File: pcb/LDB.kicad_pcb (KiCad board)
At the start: 2 copper layers, 77.2 x 50.8 mm, 79 parts, among them J1 Conn_01x10_Socket, J10 Conn_01x04_Socket, J11 Conn_01x03_Pin, J12 Conn_01x03_Pin, J13 Conn_01x03_Pin, J14 Conn_01x10_Socket, J2 Conn_01x02_Pin, J3 Conn_01x10_Socket, J4 Conn_02x02_Counter_Clockwise, J5 Conn_02x02_Counter_Clockwise, J6 Conn_02x02_Counter_Clockwise, J7 Conn_02x02_Counter_Clockwise, J8 Conn_02x02_Counter_Clockwise, J9 Conn_02x02_Counter_Clockwise, Q1 MMBFJ113, Q10 MMBFJ113, Q11 MMBFJ113, Q12 MMBFJ113, Q13 MMBFJ113, Q14 MMBFJ113, Q15 MMBFJ113, Q16 MMBFJ113, Q17 MMBFJ113, Q2 MMBFJ113, Q3 MMBFJ113, Q4 MMBFJ113, Q5 MMBFJ113, Q6 MMBFJ113, Q7 MMBFJ113, Q8 MMBFJ113, Q9 MMBFJ113, U1 4543

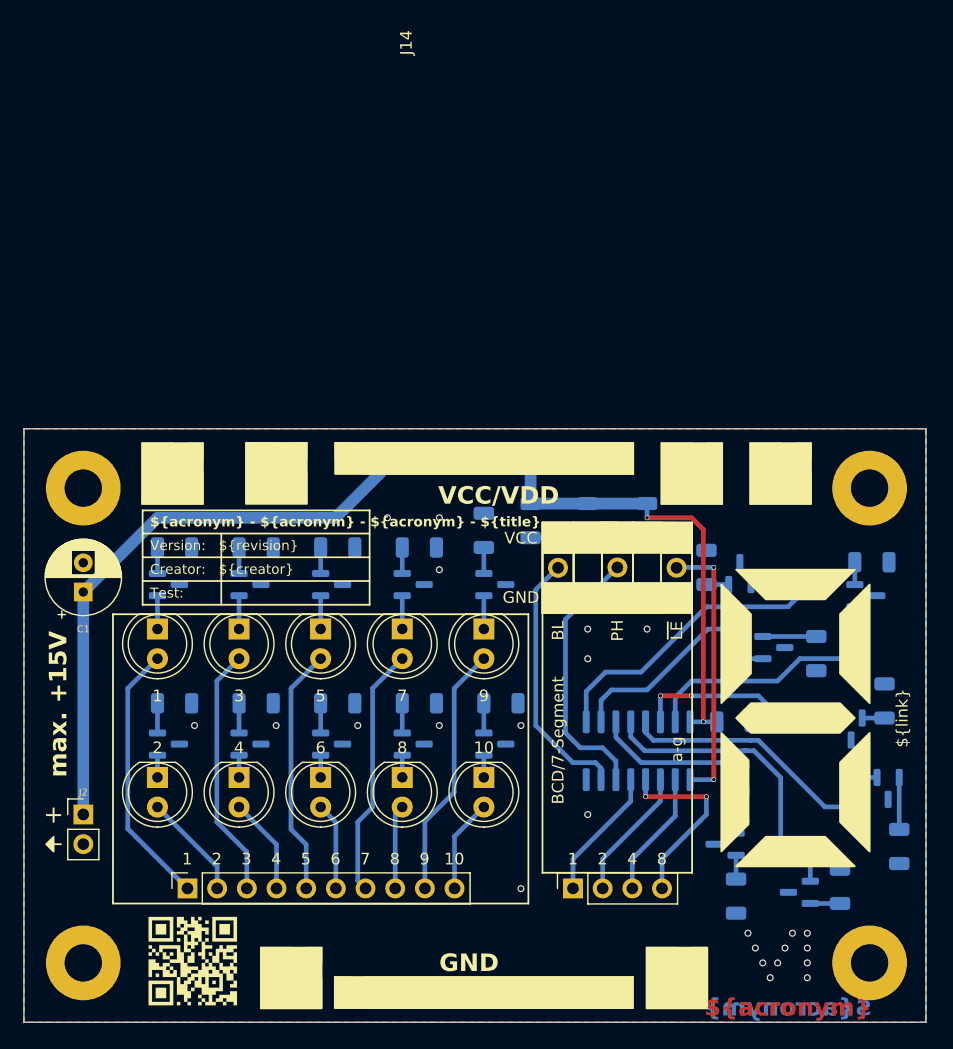
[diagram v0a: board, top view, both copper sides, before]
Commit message: Adapt edge cuts and dimensioning
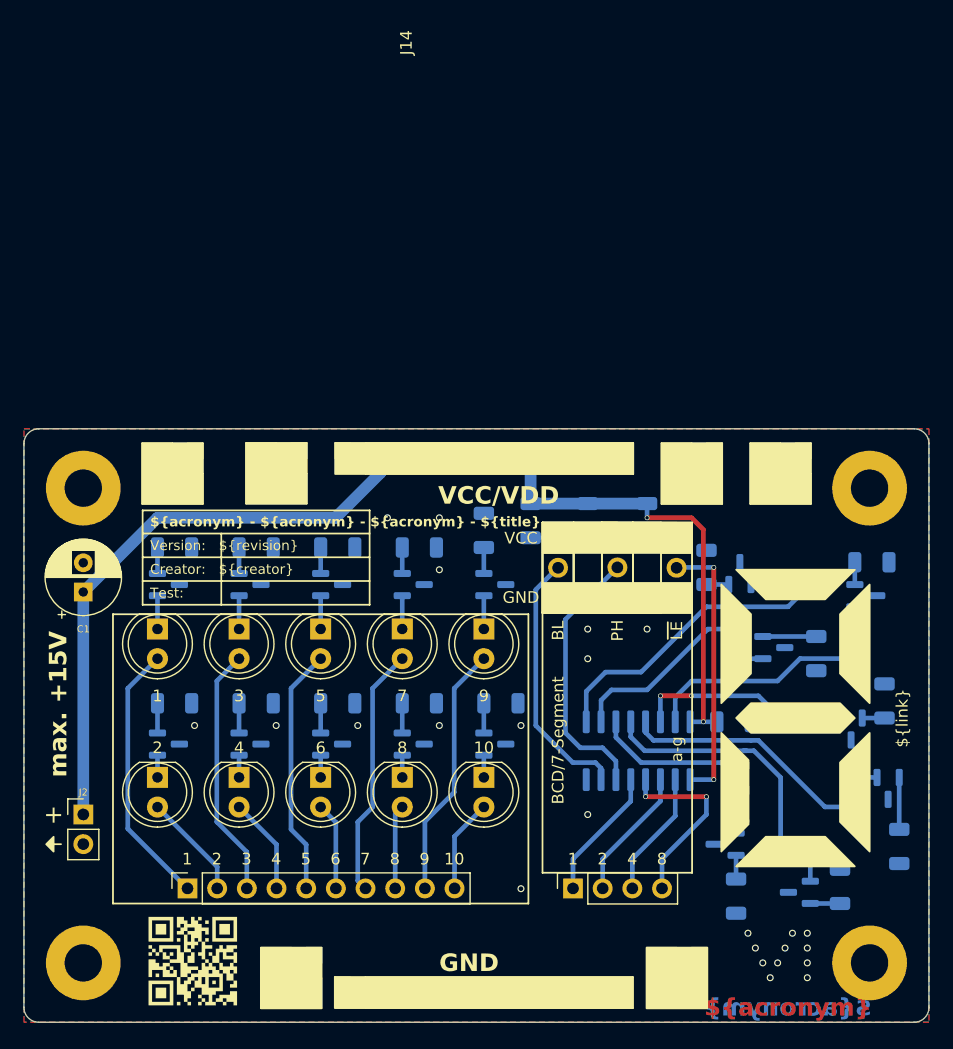
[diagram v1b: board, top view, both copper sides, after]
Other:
- board size 77.2 x 50.8 mm -> 77.5 x 50.8 mm
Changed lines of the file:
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@@
   (gr_rect (start 157.42 84.2275) (end 170.225 86.8275)
     (stroke (width 0.15) (type solid)) (fill solid) (layer "F.SilkS"))
-  (gr_rect (start 113.03 76.2) (end 190.246 127)
-    (stroke (width 0.1) (type default)) (fill none) (layer "Edge.Cuts"))
+  (gr_arc (start 114.3 127) (mid 113.401974 126.628026) (end 113.03 125.73)
+    (stroke (width 0.1) (type default)) (layer "Edge.Cuts"))
+  (gr_arc (start 190.5 125.73) (mid 190.128026 126.628026) (end 189.23 127)
+    (stroke (width 0.1) (type default)) (layer "Edge.Cuts"))
+  (gr_arc (start 189.23 76.2) (mid 190.128026 76.571974) (end 190.5 77.47)
+    (stroke (width 0.1) (type default)) (layer "Edge.Cuts"))
+  (gr_line (start 189.23 76.2) (end 114.3 76.2)
+    (stroke (width 0.1) (type default)) (layer "Edge.Cuts"))
+  (gr_line (start 114.3 127) (end 189.23 127)
+    (stroke (width 0.1) (type default)) (layer "Edge.Cuts"))
+  (gr_arc (start 113.03 77.47) (mid 113.401974 76.571974) (end 114.3 76.2)
+    (stroke (width 0.1) (type default)) (layer "Edge.Cuts"))
+  (gr_line (start 113.03 77.47) (end 113.03 125.73)
+    (stroke (width 0.1) (type default)) (layer "Edge.Cuts"))
+  (gr_line (start 190.5 125.73) (end 190.5 77.47)
+    (stroke (width 0.1) (type default)) (layer "Edge.Cuts"))
   (gr_text "${acronym}" (at 178.435 125.73) (layer "F.Cu")
     (effects (font (size 1.5 1.5) (thickness 0.3) bold))
@@
   (dimension (type aligned) (layer "Dwgs.User")
     (pts (xy 113.03 76.2) (xy 113.03 127))
-    (height 1.27)
-    (gr_text "50.80" (at 110.61 101.6 90) (layer "Dwgs.User")
+    (height 3.81)
+    (gr_text "50.80" (at 108.07 101.6 90) (layer "Dwgs.User")
       (effects (font (size 1 1) (thickness 0.15)))
     )
@@
   )
   (dimension (type aligned) (layer "Dwgs.User")
-    (pts (xy 113.03 76.2) (xy 190.246 76.2))
-    (height -1.27)
-    (gr_text "77.22" (at 151.638 73.78) (layer "Dwgs.User")
+    (pts (xy 118.11 81.28) (xy 113.03 81.28))
+    (height 6.35)
+    (gr_text "5.08" (at 115.57 73.78) (layer "Dwgs.User")
+      (effects (font (size 1 1) (thickness 0.15)))
+    )
+    (format (prefix "") (suffix "") (units 3) (units_format 0) (precision 2))
+    (style (thickness 0.15) (arrow_length 1.27) (text_position_mode 0) (extension_height 0.58642) (extension_offset 0.5) keep_text_aligned)
+  )
+  (dimension (type aligned) (layer "Dwgs.User")
+    (pts (xy 113.03 76.2) (xy 190.5 76.2))
+    (height -3.81)
+    (gr_text "77.47" (at 151.765 71.24) (layer "Dwgs.User")
+      (effects (font (size 1 1) (thickness 0.15)))
+    )
+    (format (prefix "") (suffix "") (units 3) (units_format 0) (precision 2))
+    (style (thickness 0.15) (arrow_length 1.27) (text_position_mode 0) (extension_height 0.58642) (extension_offset 0.5) keep_text_aligned)
+  )
+  (dimension (type aligned) (layer "Dwgs.User")
+    (pts (xy 118.11 81.28) (xy 118.11 76.2))
+    (height -6.35)
+    (gr_text "5.08" (at 110.61 78.74 90) (layer "Dwgs.User")
       (effects (font (size 1 1) (thickness 0.15)))
     )
@@
       (pts
         (xy 113.03 76.2)
-        (xy 190.246 76.2)
-        (xy 190.246 127)
+        (xy 190.5 76.2)
+        (xy 190.5 127)
         (xy 113.03 127)
       )

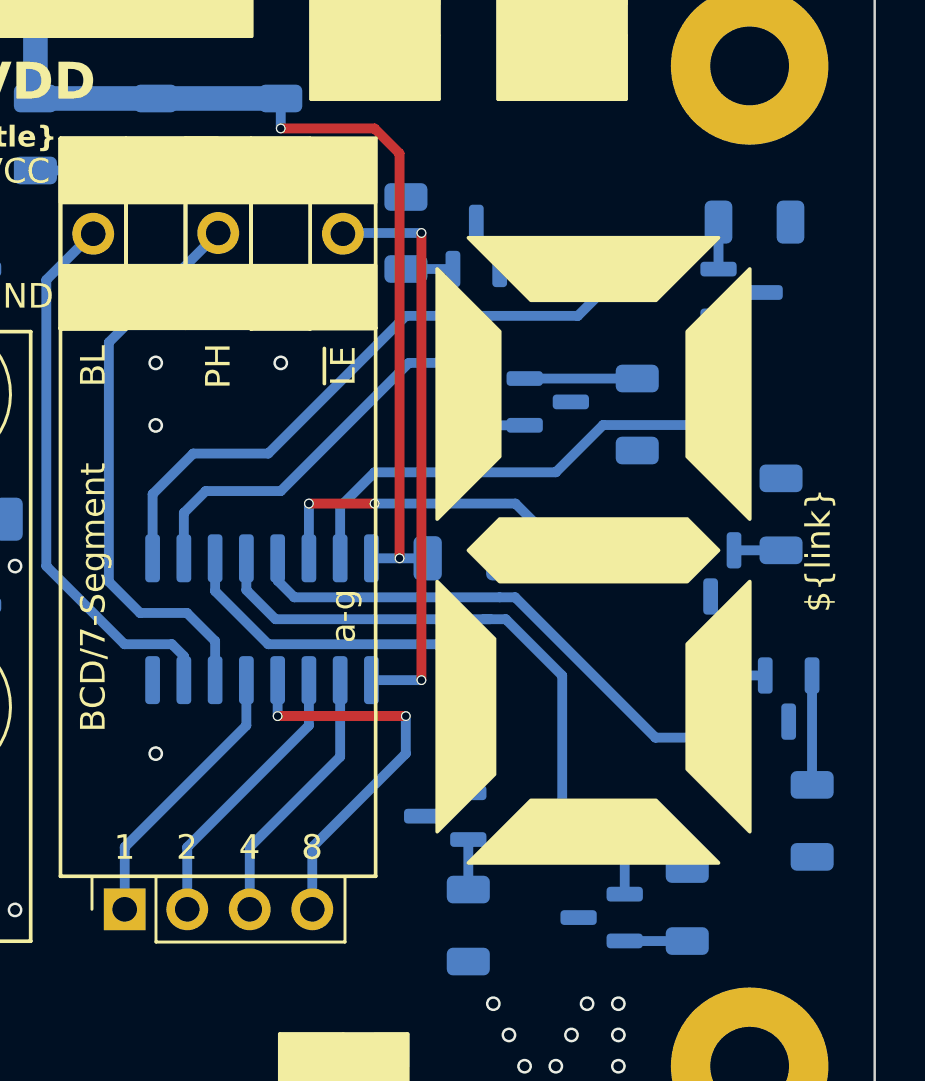
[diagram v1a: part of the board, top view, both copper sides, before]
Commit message: Swap led positions
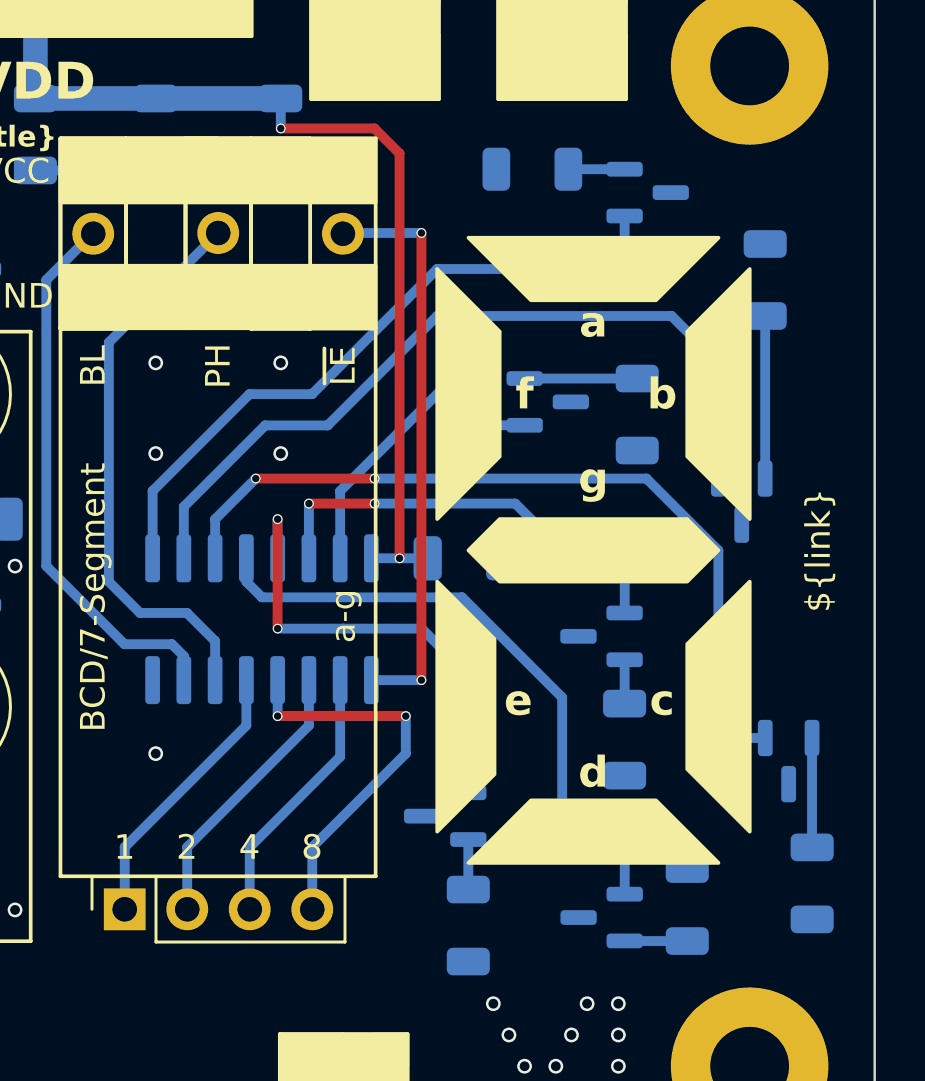
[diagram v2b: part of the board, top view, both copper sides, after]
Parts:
- moved R4 11.1 mm to (180.3, 108.7), turned to -90 degrees
- moved Q6 8.50 mm to (185.1, 99.0), turned to -90 degrees
- moved Q7 7.29 mm to (181.3, 86.4), turned to 0 degrees
- moved R10 5.75 mm to (176.6, 85.5), turned to 180 degrees
- moved Q1 5.12 mm to (179.4, 104.5), turned to 180 degrees
- moved D6 2.55 mm to (184.2, 95.9), turned to 90 degrees
- moved D5 2.55 mm to (184.2, 108.6), turned to 90 degrees
- moved R8 2.54 mm to (188.0, 114.5)
- moved D7 2.54 mm to (180.3, 89.5), turned to 180 degrees
- moved Q5 2.54 mm to (187.0, 109.5)
- moved R9 2.39 mm to (186.1, 90.0), turned to 90 degrees
- renumbered D6 to D2, D5 to D3, D3 to D5, D2 to D6, Q6 to Q2, Q5 to Q3, Q3 to Q5, Q2 to Q6, R9 to R5, R8 to R6, R6 to R8, R5 to R9
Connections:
- D2 pad 2: /b -> /f
- D3 pad 2: /c -> /e
- D5 pad 2: /e -> /c
- D6 pad 2: /f -> /b
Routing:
- net /c: track 13.0 -> 29.0 mm, vias 0 -> 2
- net /b: track 15.9 -> 27.8 mm
- net /f: track 18.8 -> 10.1 mm
- net /e: track 21.5 -> 14.4 mm, vias 0 -> 2
- net Net-(Q6-S): track 1.91 -> 6.60 mm
- net /a: track 25.6 -> 23.1 mm
- net /d: track 22.2 -> 21.2 mm
- net GND: vias 24 -> 25
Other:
- board text added: "a"
- board text added: "b"
- board text added: "c"
- board text added: "d"
- board text added: "e"
- board text added: "f"
- board text added: "g"

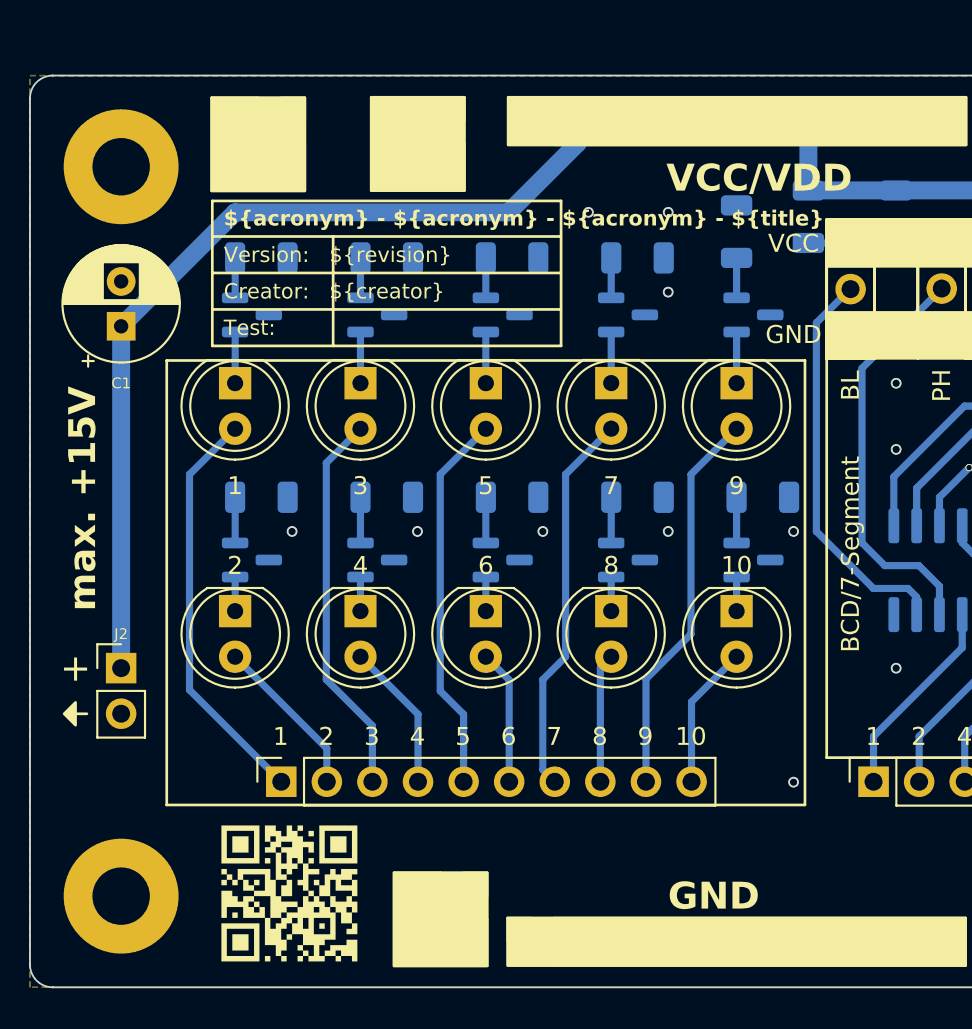
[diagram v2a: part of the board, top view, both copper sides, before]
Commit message: Add reverse polarity protection
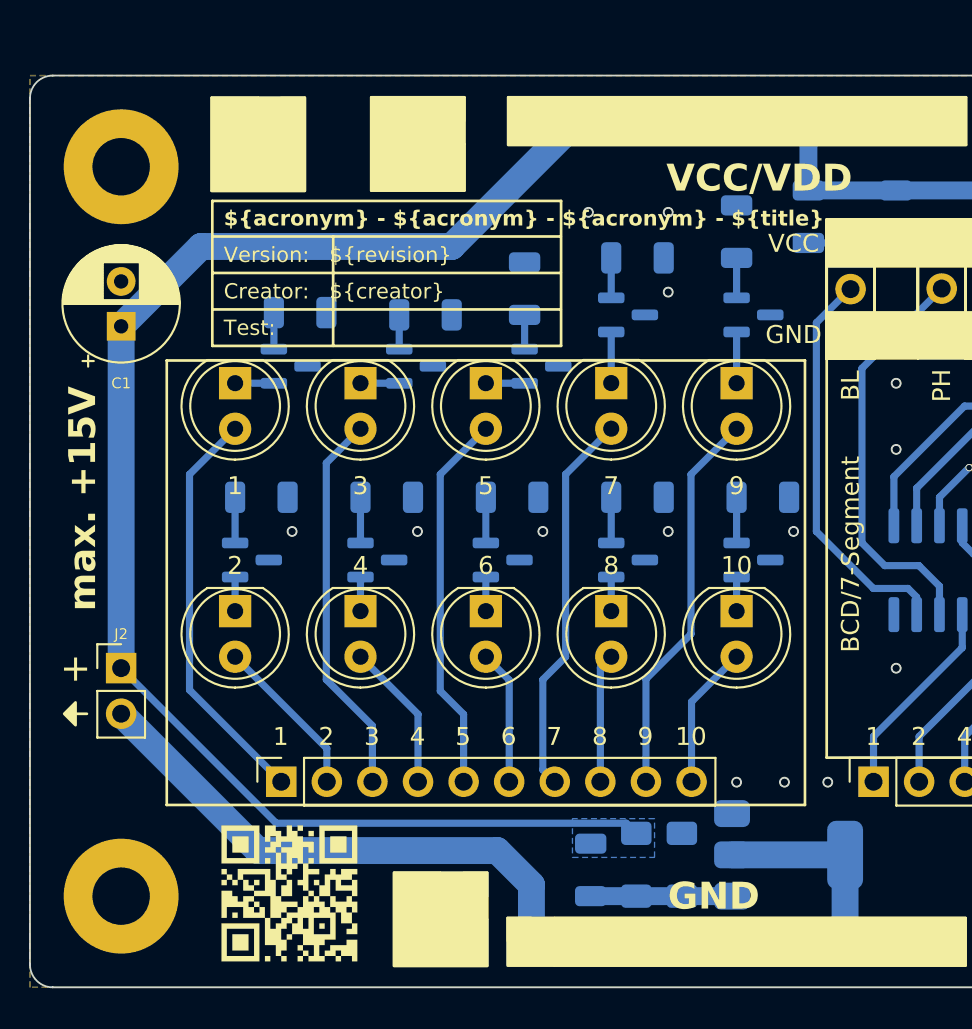
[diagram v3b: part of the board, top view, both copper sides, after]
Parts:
- added D18: BAT43, Diode_SMD:D_MiniMELF, B.Cu at (146.8, 120.2)
- added D19: BZ5V1, Diode_SMD:D_MiniMELF, B.Cu at (149.4, 120.2)
- added Q18: BUK7880-55A, Package_TO_SOT_SMD:SOT-223-3_TabPin2, B.Cu at (155.3, 119.6)
- added R21: 1k, Resistor_SMD:R_1206_3216Metric, B.Cu at (144.3, 120.5)
- moved FID2 7.76 mm to (163.3, 119.8)
- moved R12 3.84 mm to (135.1, 89.5)
- moved R11 3.74 mm to (128.1, 89.4)
- moved Q9 3.58 mm to (134.5, 92.4)
- moved Q8 3.58 mm to (127.6, 92.4)
- moved Q10 3.58 mm to (141.5, 92.4)
- moved FID3 2.08 mm to (128.3, 123.6)
- moved R13 1.85 mm to (140.6, 88.1), turned to 90 degrees
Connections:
- J2 pad 2: GND -> Net-(J2-Pin_2)
- J3 pad 1: GND -> Net-(J2-Pin_2)
- J3 pad 10: GND -> Net-(J2-Pin_2)
- J3 pad 2: GND -> Net-(J2-Pin_2)
- J3 pad 3: GND -> Net-(J2-Pin_2)
- J3 pad 4: GND -> Net-(J2-Pin_2)
- J3 pad 5: GND -> Net-(J2-Pin_2)
- J3 pad 6: GND -> Net-(J2-Pin_2)
- J3 pad 7: GND -> Net-(J2-Pin_2)
- J3 pad 8: GND -> Net-(J2-Pin_2)
- J3 pad 9: GND -> Net-(J2-Pin_2)
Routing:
- net Net-(J2-Pin_2): track 0.00 -> 41.2 mm
- net VCC: track 89.0 -> 120.8 mm
- net Net-(D18-A): track 0.00 -> 7.87 mm
- net Net-(D10-K): track 2.86 -> 2.16 mm
- net Net-(D8-K): track 2.86 -> 2.16 mm
- net Net-(D9-K): track 2.86 -> 2.16 mm
- net GND: vias 25 -> 27
- added copper zone on B.Cu, net Net-(J2-Pin_2)
